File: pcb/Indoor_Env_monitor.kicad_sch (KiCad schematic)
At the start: 6 parts, among them J1 JST SH 4-Pin, J2 Conn_01x08, U1 ESP32-WROOM-32D, U2 BQ24090DGQ

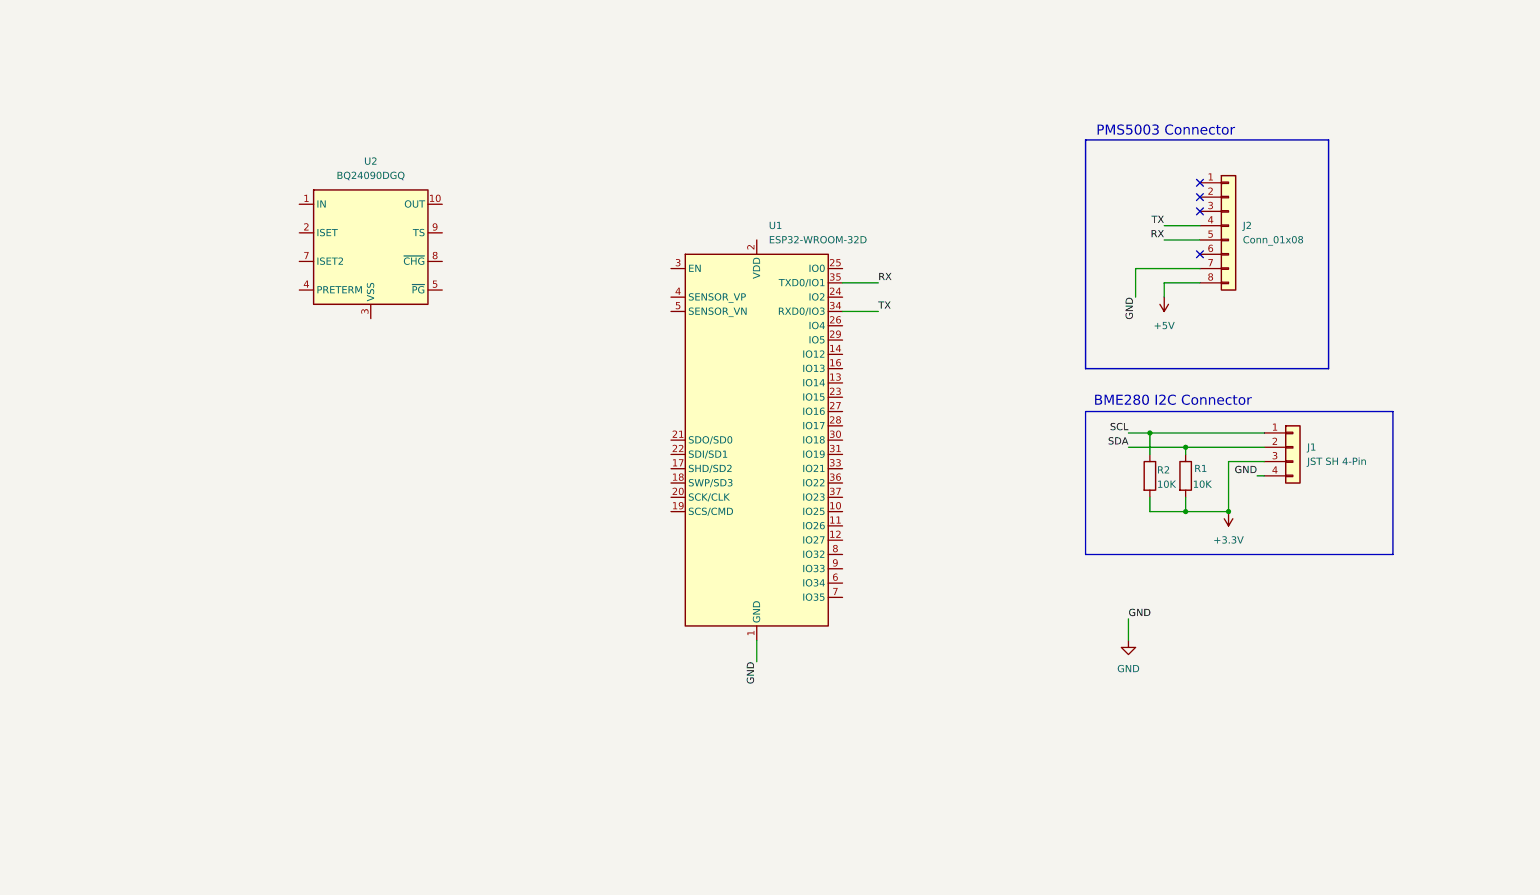
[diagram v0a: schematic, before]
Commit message: Created the schematic and PCB
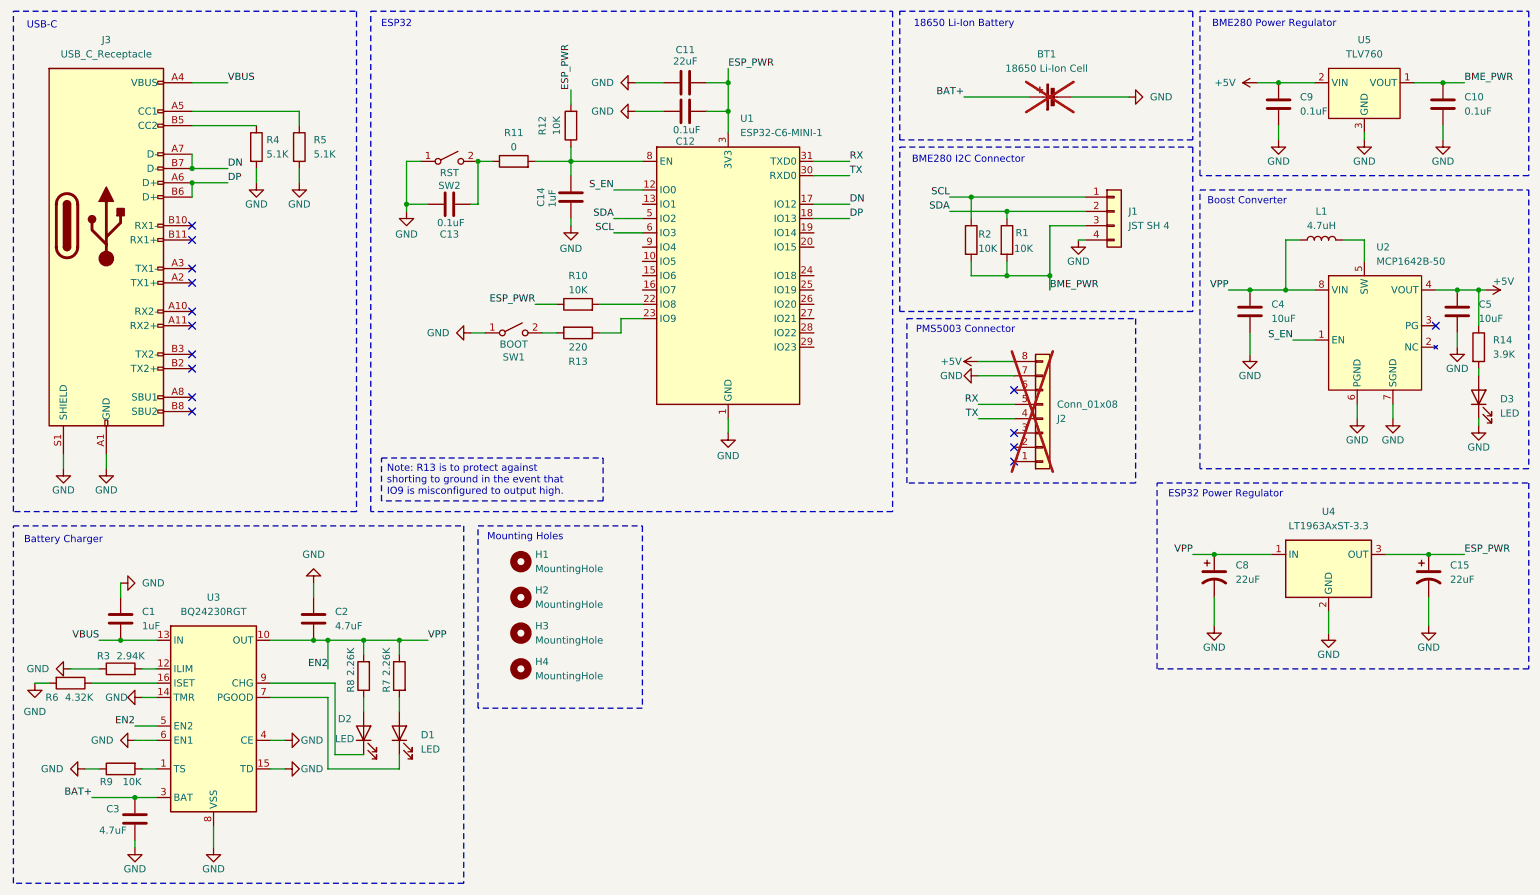
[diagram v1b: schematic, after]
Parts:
- removed U1: ESP32-WROOM-32D, RF_Module:ESP32-WROOM-32D, symbol RF_Module:ESP32-WROOM-32D
- removed U2: BQ24090DGQ, Package_SO:HVSSOP-10-1EP_3x3mm_P0.5mm_EP1.57x1.88mm_ThermalVias, symbol Battery_Management:BQ24090DGQ
- added BT1: 18650 Li-Ion Cell, Connector_JST:JST_PH_S2B-PH-K_1x02_P2.00mm_Horizontal, symbol Device:Battery_Cell
- added C1, C14: 1uF, Capacitor_SMD:C_0402_1005Metric_Pad0.74x0.62mm_HandSolder, symbol Device:C
- added C10, C12, C13, C9: 0.1uF, Capacitor_SMD:C_0402_1005Metric_Pad0.74x0.62mm_HandSolder, symbol Device:C
- added C11: 22uF, Capacitor_SMD:C_0402_1005Metric_Pad0.74x0.62mm_HandSolder, symbol Device:C
- added C15, C8: 22uF, Capacitor_SMD:C_0402_1005Metric_Pad0.74x0.62mm_HandSolder, symbol Device:C_Polarized_US
- added C2, C3: 4.7uF, Capacitor_SMD:C_0402_1005Metric_Pad0.74x0.62mm_HandSolder, symbol Device:C
- added C4, C5: 10uF, Capacitor_SMD:C_0402_1005Metric_Pad0.74x0.62mm_HandSolder, symbol Device:C
- added D1, D2, D3: LED, LED_SMD:LED_0402_1005Metric_Pad0.77x0.64mm_HandSolder, symbol Device:LED
- added H1, H2, H3, H4: MountingHole, MountingHole:MountingHole_3.2mm_M3, symbol Mechanical:MountingHole
- added J3: USB_C_Receptacle, Connector_USB:USB_C_Receptacle_G-Switch_GT-USB-7010ASV, symbol Connector:USB_C_Receptacle
- added L1: 4.7uH, Inductor_SMD:L_Coilcraft_LPS4018, symbol Device:L
- added R10, R12, R9: 10K, Resistor_SMD:R_0402_1005Metric_Pad0.72x0.64mm_HandSolder, symbol Device:R
- added R11: 0, Resistor_SMD:R_0402_1005Metric_Pad0.72x0.64mm_HandSolder, symbol Device:R
- added R13: 220, Resistor_SMD:R_0402_1005Metric_Pad0.72x0.64mm_HandSolder, symbol Device:R
- added R14: 3.9K, Resistor_SMD:R_0402_1005Metric_Pad0.72x0.64mm_HandSolder, symbol Device:R
- added R3: 2.94K, Resistor_SMD:R_0402_1005Metric_Pad0.72x0.64mm_HandSolder, symbol Device:R
- added R4, R5: 5.1K, Resistor_SMD:R_0402_1005Metric_Pad0.72x0.64mm_HandSolder, symbol Device:R
- added R6: 4.32K, Resistor_SMD:R_0402_1005Metric_Pad0.72x0.64mm_HandSolder, symbol Device:R
- added R7, R8: 2.26K, Resistor_SMD:R_0402_1005Metric_Pad0.72x0.64mm_HandSolder, symbol Device:R
- added SW1: BOOT, Button_Switch_SMD:SW_Push_1P1T-SH_NO_CK_KMR2xxG, symbol Switch:SW_SPST
- added SW2: RST, Button_Switch_SMD:SW_Push_1P1T-SH_NO_CK_KMR2xxG, symbol Switch:SW_SPST
- added U1: ESP32-C6-MINI-1, RF_Module:ESP32-C6-MINI-1, symbol RF_Module:ESP32-C6-MINI-1
- added U2: MCP1642B-50, Package_SO:MSOP-8_3x3mm_P0.65mm, symbol 1a_Regulator_Switchting:MCP1642B/D-XX
- added U3: BQ24230RGT, Package_DFN_QFN:VQFN-16-1EP_3x3mm_P0.5mm_EP1.68x1.68mm_ThermalVias, symbol Power_Management:BQ24230RGT
- added U4: LT1963AxST-3.3, Package_TO_SOT_SMD:SOT-223-3_TabPin2, symbol Regulator_Linear:LT1963AxST-3.3
- added U5: TLV760, Package_TO_SOT_SMD:SOT-23_Handsoldering, symbol 1a_Regulator_Linear:TLV760
- J1: value JST SH 4-Pin -> JST SH 4; footprint (none) -> Connector_JST:JST_SH_BM04B-SRSS-TB_1x04-1MP_P1.00mm_Vertical
- J2: footprint (none) -> Connector_Molex:Molex_PicoBlade_53047-0810_1x08_P1.25mm_Vertical; now not fitted
- R1, R2: footprint (none) -> Resistor_SMD:R_0402_1005Metric_Pad0.72x0.64mm_HandSolder
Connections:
- net +5V: now also C5.1, C9.1, R14.1, U2.4 (VOUT), U5.2 (VIN)
- net GND: now also BT1.2 (-), C1.1, C10.2, C11.1, C12.1, C13.1, C14.2, C15.2, C2.1, C3.2, C4.2, C5.2, C8.2, C9.2, D3.1 (K), J3.A1 (GND), J3.A12 (GND), J3.B1 (GND), J3.B12 (GND), J3.S1 (SHIELD), R3.1, R4.2, R5.2, R6.2, R9.1, SW1.1 (A), SW2.1 (A), U1.1 (GND), U1.11 (GND), U1.14 (GND), U1.2 (GND), U1.36 (GND), U1.37 (GND), U1.38 (GND), U1.39 (GND), U1.40 (GND), U1.41 (GND), U1.42 (GND), U1.43 (GND), U1.44 (GND), U1.45 (GND), U1.46 (GND), U1.47 (GND), U1.48 (GND), U1.49 (GND), U1.50 (GND), U1.51 (GND), U1.52 (GND), U1.53 (GND), U2.6 (PGND), U2.7 (SGND), U3.14 (TMR), U3.15 (TD), U3.17 (VSS), U3.4 (CE), U3.6 (EN1), U3.8 (VSS), U4.2 (GND), U5.3 (GND)
- net RX: now also U1.31 (TXD0)
- net SCL: now also U1.6 (IO3)
- net SDA: now also U1.5 (IO2)
- net TX: now also U1.30 (RXD0)
- net +3.3V renamed BME_PWR
- net BME_PWR: now also C10.1, U5.1 (VOUT)
- new net: C13.2, R11.1, SW2.2 (B)
- new net: D1.1 (K), U3.7 (PGOOD)
- new net: D1.2 (A), R7.2
- new net: J3.A5 (CC1), R5.1
- new net: L1.2, U2.5 (SW)
- new net: C14.1, R11.2, R12.1, U1.8 (EN)
- new net: J3.B5 (CC2), R4.1
- new net: D2.1 (K), U3.9 (CHG)
- new net: D2.2 (A), R8.1
- new net: D3.2 (A), R14.2
- new net: R10.2, U1.22 (IO8)
- new net: R9.2, U3.1 (TS)
- new net: R3.2, U3.12 (ILIM)
- new net: R6.1, U3.16 (ISET)
- new net: R13.1, U1.23 (IO9)
- new net: R13.2, SW1.2 (B)
- new net BAT+: BT1.1 (+), C3.1, U3.2 (BAT), U3.3 (BAT)
- new net DN: J3.A7 (D-), J3.B7 (D-), U1.17 (IO12)
- new net DP: J3.A6 (D+), J3.B6 (D+), U1.18 (IO13)
- new net EN2: C2.2, C4.1, C8.1, L1.1, R7.1, R8.2, U2.8 (VIN), U3.10 (OUT), U3.11 (OUT), U3.5 (EN2), U4.1 (IN)
- new net ESP_PWR: C11.2, C12.2, C15.1, R10.1, R12.2, U1.3 (3V3), U4.3 (OUT)
- new net S_EN: U1.12 (IO0), U2.1 (EN)
- new net VBUS: C1.2, J3.A4 (VBUS), J3.A9 (VBUS), J3.B4 (VBUS), J3.B9 (VBUS), U3.13 (IN)
- no-connect marks 4 -> 15
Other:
- note added: "18650 Li-Ion Battery"
- note added: "BME280 Power Regulator"
- note added: "Battery Charger"
- note added: "Boost Converter"
- note added: "ESP32"
- note added: "ESP32 Power Regulator"
- note added: "Mounting Holes"
- note added: "USB-C"
- moved on the sheet: J1, R1, R2

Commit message: Little change
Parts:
- J2: now fitted
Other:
- title: (none) -> Indoor Environment Monitor
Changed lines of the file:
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@@
 	(generator_version "9.0")
 	(paper "A4")
+	(title_block
+		(title "Indoor Environment Monitor")
+		(date "2025-10-17")
+		(rev "1.0")
+	)
 	(rectangle
 		(start 224.79 13.97)
@@
 		(in_bom yes)
 		(on_board yes)
-		(dnp yes)
+		(dnp no)
 		(property "Reference" "J2"
 			(at 199.39 86.3601 0)
